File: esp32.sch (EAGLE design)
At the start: 63 parts, among them IC1 PEC11R-4230K-S00243D, IC2 AD8532ARZ, T1 BST82-1, T2 BST82-1, U1 ESP32-WROOM-32D, X1 JST-XH-02-PIN-LONG-PAD, X2 JST-XH-03-PIN-LONG-PAD, X3 JST-XH-03-PIN-LONG-PAD, X4 JST-XH-02-PIN-LONG-PAD

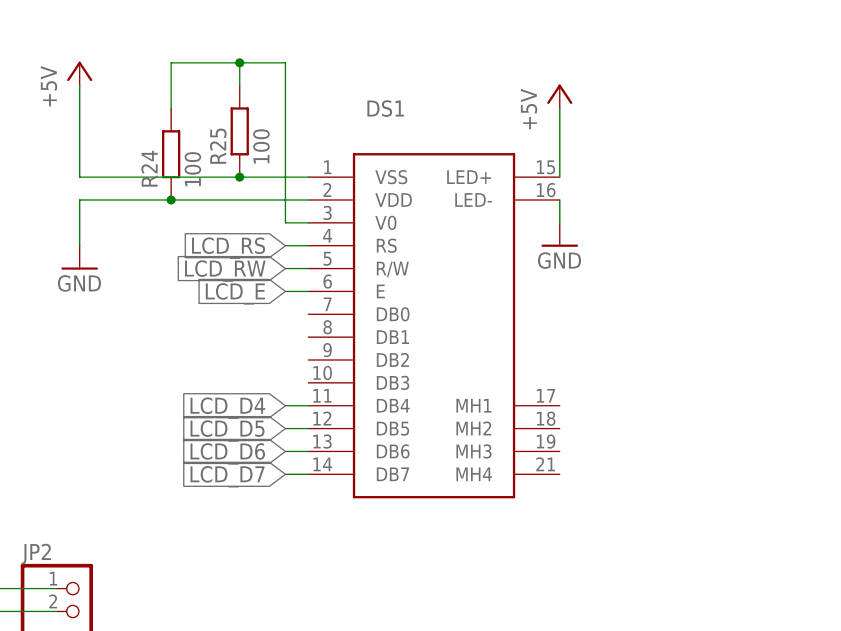
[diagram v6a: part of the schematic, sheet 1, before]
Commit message: Added dimmer for lcd and starting redouting to 18mil
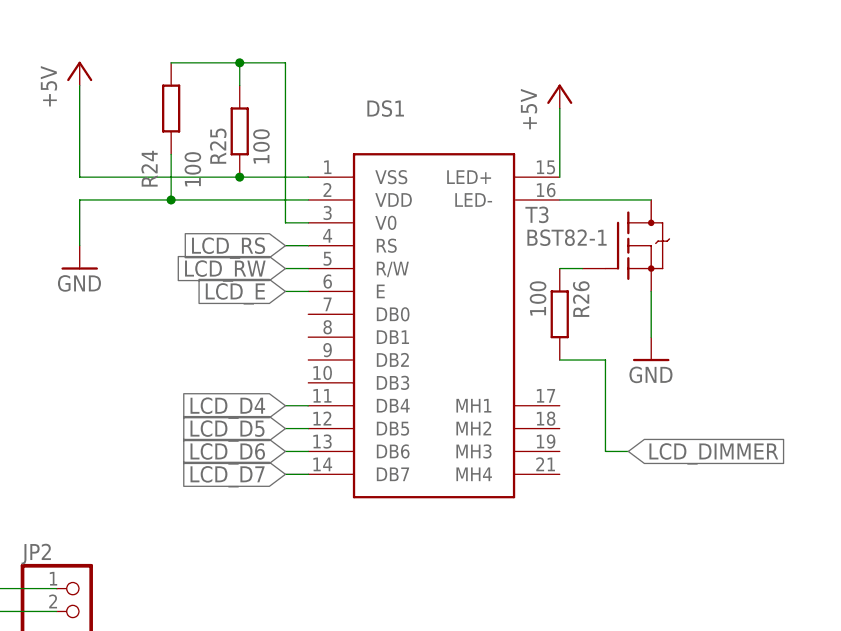
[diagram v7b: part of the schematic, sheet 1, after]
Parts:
- added R26: 100, rcl:R-EU_R0603
- added T3: BST82-1, Test:BST82-1
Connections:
- new net LCD_DIMMER: R26.2
- new net N$16: R26.1, T3.G
- new net N$18: DS1.LED-, T3.D
- net GND: now also T3.S; no longer DS1.LED-
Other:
- moved on the sheet: R24
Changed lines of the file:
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@@
 <part name="R24" library="rcl" library_urn="urn:adsk.eagle:library:334" deviceset="R-EU_" device="R0603" package3d_urn="urn:adsk.eagle:package:23555/3" value="100"/>
 <part name="R25" library="rcl" library_urn="urn:adsk.eagle:library:334" deviceset="R-EU_" device="R0603" package3d_urn="urn:adsk.eagle:package:23555/3" value="100"/>
+<part name="T3" library="Test" library_urn="urn:adsk.eagle:library:24473944" deviceset="BST82-1" device="" package3d_urn="urn:adsk.eagle:package:11819622/2"/>
+<part name="R26" library="rcl" library_urn="urn:adsk.eagle:library:334" deviceset="R-EU_" device="R0603" package3d_urn="urn:adsk.eagle:package:23555/3" value="100"/>
 </parts>
 <sheets>
@@
 <attribute name="VALUE" x="233.68" y="149.86" size="1.778" layer="96" rot="R90"/>
 </instance>
-<instance part="GND21" gate="1" x="236.22" y="137.16" smashed="yes">
-<attribute name="VALUE" x="233.68" y="134.62" size="1.778" layer="96"/>
+<instance part="GND21" gate="1" x="246.38" y="124.46" smashed="yes">
+<attribute name="VALUE" x="243.84" y="121.92" size="1.778" layer="96"/>
 </instance>
 <instance part="GND22" gate="1" x="182.88" y="134.62" smashed="yes">
@@
 <attribute name="VALUE" x="141.224" y="48.641" size="1.778" layer="96"/>
 </instance>
-<instance part="R24" gate="G$1" x="193.04" y="147.32" smashed="yes" rot="R90">
+<instance part="R24" gate="G$1" x="193.04" y="152.4" smashed="yes" rot="R90">
 <attribute name="NAME" x="191.5414" y="143.51" size="1.778" layer="95" rot="R90"/>
 <attribute name="VALUE" x="196.342" y="143.51" size="1.778" layer="96" rot="R90"/>
@@
 <attribute name="NAME" x="199.1614" y="146.05" size="1.778" layer="95" rot="R90"/>
 <attribute name="VALUE" x="203.962" y="146.05" size="1.778" layer="96" rot="R90"/>
+</instance>
+<instance part="T3" gate="G$1" x="243.84" y="137.16" smashed="yes">
+<attribute name="VALUE" x="232.41" y="137.16" size="1.778" layer="96"/>
+<attribute name="NAME" x="232.41" y="139.7" size="1.778" layer="95"/>
+</instance>
+<instance part="R26" gate="G$1" x="236.22" y="129.54" smashed="yes" rot="R270">
+<attribute name="NAME" x="237.7186" y="133.35" size="1.778" layer="95" rot="R270"/>
+<attribute name="VALUE" x="232.918" y="133.35" size="1.778" layer="96" rot="R270"/>
 </instance>
 </instances>
@@
 </segment>
 <segment>
-<pinref part="GND21" gate="1" pin="GND"/>
-<pinref part="DS1" gate="G$1" pin="LED-"/>
-<wire x1="236.22" y1="139.7" x2="236.22" y2="142.24" width="0.1524" layer="91"/>
-</segment>
-<segment>
 <pinref part="DS1" gate="G$1" pin="VDD"/>
 <pinref part="GND22" gate="1" pin="GND"/>
@@
 <pinref part="R24" gate="G$1" pin="1"/>
 <junction x="193.04" y="142.24"/>
+<wire x1="193.04" y1="142.24" x2="193.04" y2="147.32" width="0.1524" layer="91"/>
 </segment>
 <segment>
@@
 <junction x="50.8" y="17.78"/>
 </segment>
+<segment>
+<pinref part="T3" gate="G$1" pin="S"/>
+<pinref part="GND21" gate="1" pin="GND"/>
+<wire x1="246.38" y1="132.08" x2="246.38" y2="127" width="0.1524" layer="91"/>
+</segment>
 </net>
 <net name="+5V" class="0">
@@
 <wire x1="205.74" y1="139.7" x2="205.74" y2="157.48" width="0.1524" layer="91"/>
 <pinref part="R24" gate="G$1" pin="2"/>
-<wire x1="193.04" y1="152.4" x2="193.04" y2="157.48" width="0.1524" layer="91"/>
 <wire x1="193.04" y1="157.48" x2="200.66" y2="157.48" width="0.1524" layer="91"/>
 <pinref part="R25" gate="G$1" pin="2"/>
@@
 </segment>
 </net>
+<net name="N$16" class="0">
+<segment>
+<wire x1="236.22" y1="134.62" x2="238.76" y2="134.62" width="0.1524" layer="91"/>
+<pinref part="T3" gate="G$1" pin="G"/>
+<pinref part="R26" gate="G$1" pin="1"/>
+</segment>
+</net>
+<net name="N$18" class="0">
+<segment>
+<pinref part="DS1" gate="G$1" pin="LED-"/>
+<pinref part="T3" gate="G$1" pin="D"/>
+<wire x1="236.22" y1="142.24" x2="246.38" y2="142.24" width="0.1524" layer="91"/>
+</segment>
+</net>
+<net name="LCD_DIMMER" class="0">
+<segment>
+<pinref part="R26" gate="G$1" pin="2"/>
+<wire x1="236.22" y1="124.46" x2="241.3" y2="124.46" width="0.1524" layer="91"/>
+<wire x1="241.3" y1="124.46" x2="241.3" y2="114.3" width="0.1524" layer="91"/>
+<wire x1="241.3" y1="114.3" x2="243.84" y2="114.3" width="0.1524" layer="91"/>
+<label x="243.84" y="114.3" size="1.778" layer="95" xref="yes"/>
+</segment>
+</net>

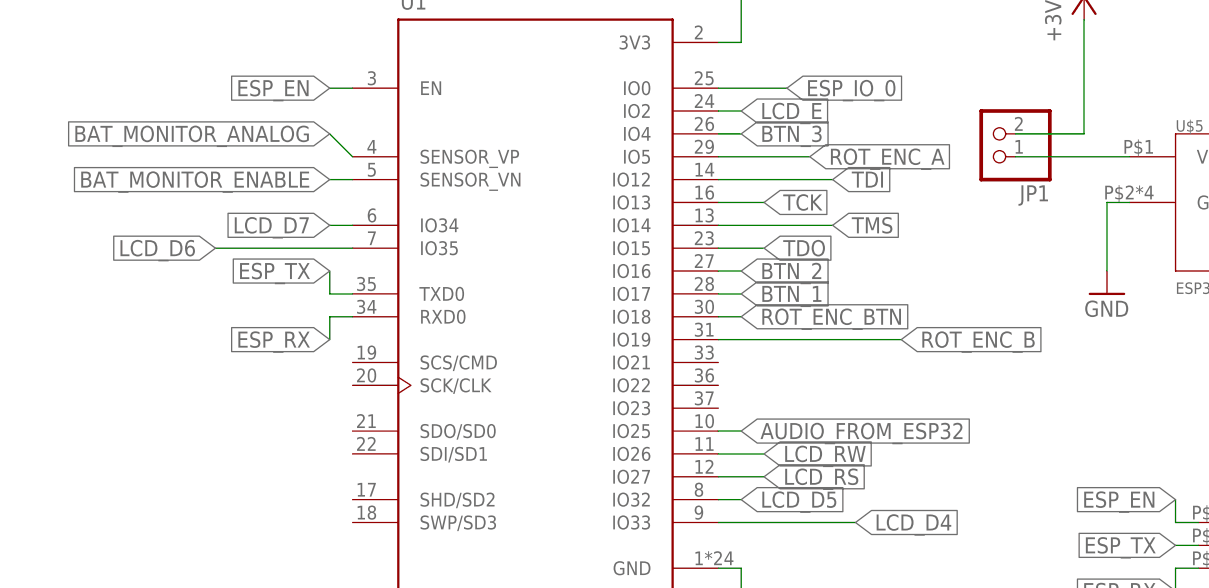
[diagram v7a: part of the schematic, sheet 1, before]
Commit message: Kopplade alla signaler, ska göra om footprint för LCD och sen sätta på 3.3V regulator och sen borde den vara komplett!
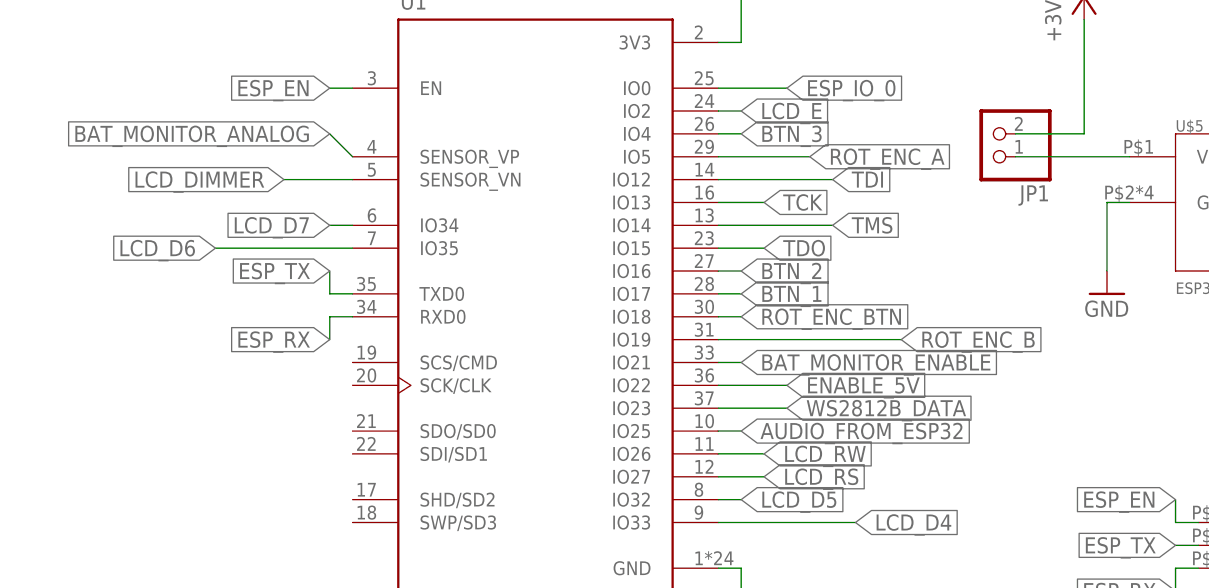
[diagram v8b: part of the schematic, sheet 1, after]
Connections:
- net BAT_MONITOR_ENABLE: now also U1.IO21; no longer U1.SENSOR_VN
- net ENABLE_5V: now also U1.IO22
- net LCD_DIMMER: now also U1.SENSOR_VN
- net WS2812B_DATA: now also U1.IO23
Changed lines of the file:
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@@
 <label x="208.28" y="45.72" size="1.778" layer="95" rot="R180" xref="yes"/>
+</segment>
+<segment>
+<wire x1="81.28" y1="111.76" x2="88.9" y2="111.76" width="0.1524" layer="91"/>
+<label x="88.9" y="111.76" size="1.778" layer="95" xref="yes"/>
+<pinref part="U1" gate="G$1" pin="IO22"/>
 </segment>
 </net>
@@
 <net name="BAT_MONITOR_ENABLE" class="0">
 <segment>
-<pinref part="U1" gate="G$1" pin="SENSOR_VN"/>
-<wire x1="40.64" y1="134.62" x2="38.1" y2="134.62" width="0.1524" layer="91"/>
-<label x="38.1" y="134.62" size="1.778" layer="95" rot="R180" xref="yes"/>
+<label x="83.82" y="114.3" size="1.778" layer="95" xref="yes"/>
+<pinref part="U1" gate="G$1" pin="IO21"/>
+<wire x1="81.28" y1="114.3" x2="83.82" y2="114.3" width="0.1524" layer="91"/>
 </segment>
 </net>
@@
 <label x="243.84" y="114.3" size="1.778" layer="95" xref="yes"/>
 </segment>
-</net>
+<segment>
+<label x="33.02" y="134.62" size="1.778" layer="95" rot="R180" xref="yes"/>
+</segment>
+<segment>
+<pinref part="U1" gate="G$1" pin="SENSOR_VN"/>
+<wire x1="40.64" y1="134.62" x2="33.02" y2="134.62" width="0.1524" layer="91"/>
+</segment>
+</net>
+<net name="WS2812B_DATA" class="0">
+<segment>
+<wire x1="81.28" y1="109.22" x2="88.9" y2="109.22" width="0.1524" layer="91"/>
+<label x="88.9" y="109.22" size="1.778" layer="95" xref="yes"/>
+<pinref part="U1" gate="G$1" pin="IO23"/>
+</segment>
+</net>
